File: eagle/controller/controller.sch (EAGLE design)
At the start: 6 parts, among them IC1 ATMEGA48/88/168-PU, IC2 LP2950ACZ-5.0

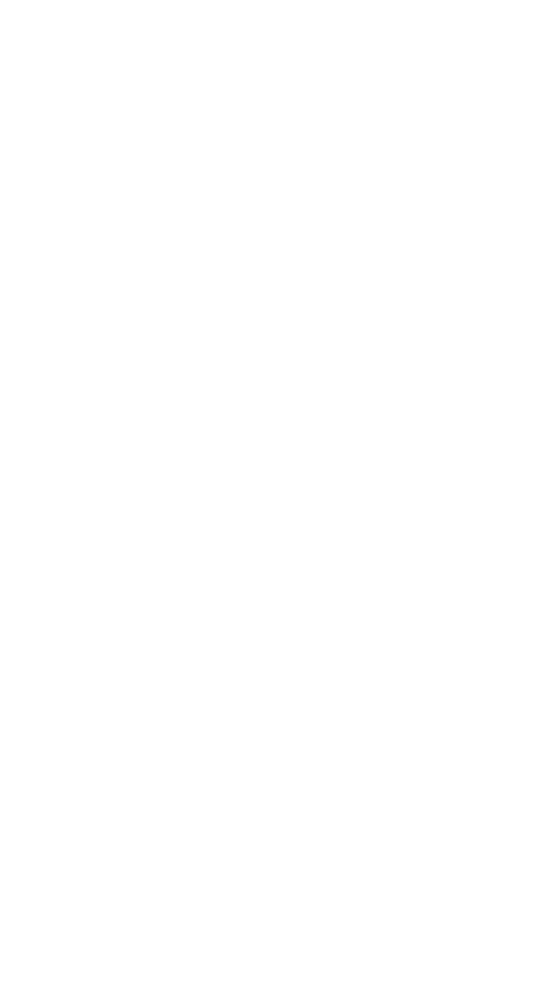
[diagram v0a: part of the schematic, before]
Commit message: Added REED for sensor switches
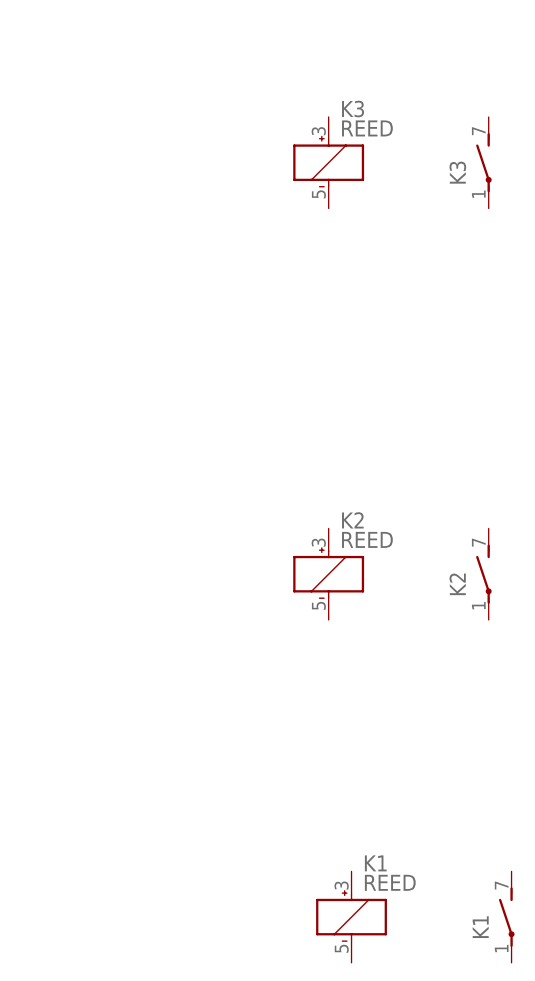
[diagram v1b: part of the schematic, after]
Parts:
- added K1, K2, K3: REED, relay:REED
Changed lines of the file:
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@@
 <part name="C2" library="resistor" deviceset="CPOL-EU" device="E2.5-7" value="10u"/>
 <part name="C3" library="resistor" deviceset="CPOL-EU" device="E2.5-7" value="10u"/>
+<part name="K1" library="relay" deviceset="REED" device=""/>
+<part name="K2" library="relay" deviceset="REED" device=""/>
+<part name="K3" library="relay" deviceset="REED" device=""/>
 </parts>
 <sheets>
@@
 <instance part="C2" gate="G$1" x="-27.94" y="68.58"/>
 <instance part="C3" gate="G$1" x="-55.88" y="68.58"/>
+<instance part="K1" gate="2" x="208.28" y="-5.08"/>
+<instance part="K1" gate="1" x="190.5" y="-5.08"/>
+<instance part="K2" gate="2" x="205.74" y="33.02"/>
+<instance part="K2" gate="1" x="187.96" y="33.02"/>
+<instance part="K3" gate="2" x="205.74" y="78.74"/>
+<instance part="K3" gate="1" x="187.96" y="78.74"/>
 </instances>
 <busses>

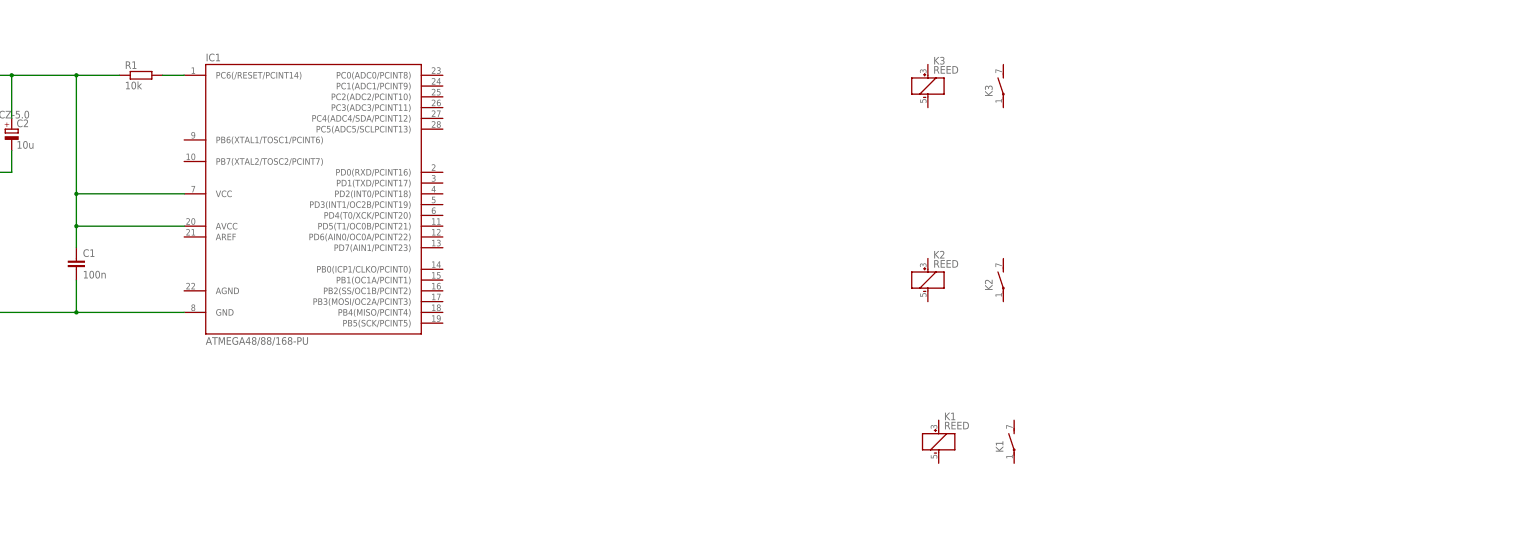
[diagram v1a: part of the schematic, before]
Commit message: Added base water sensors
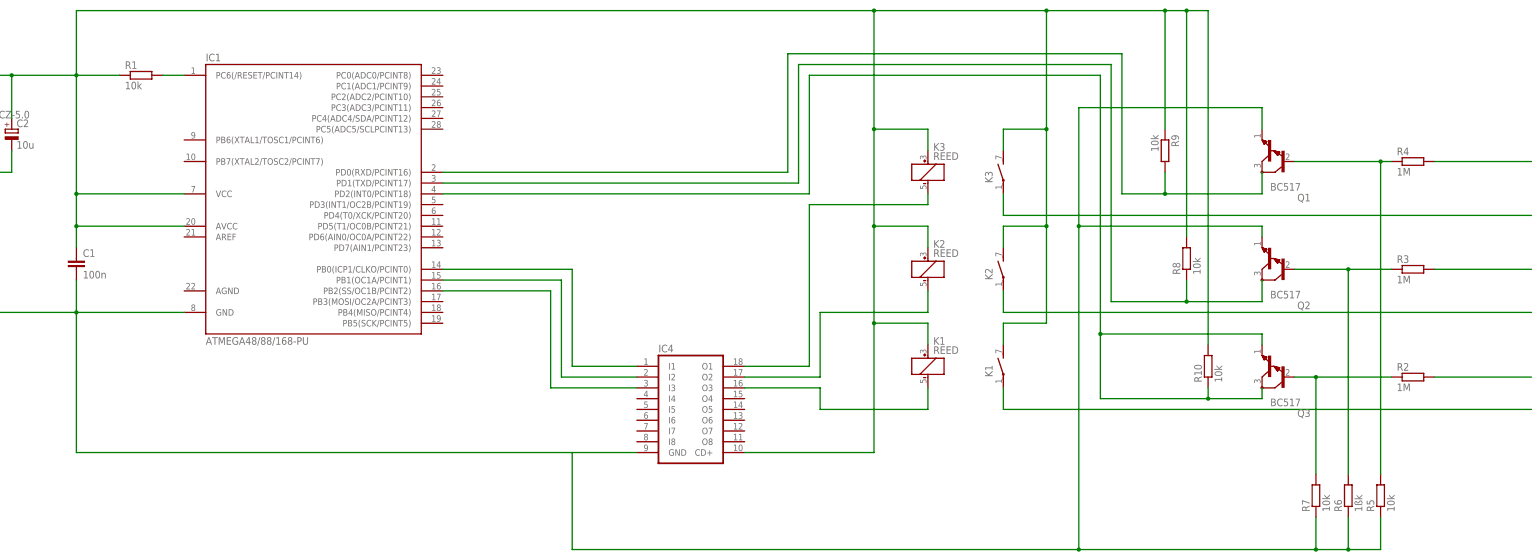
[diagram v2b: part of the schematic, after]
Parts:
- added IC4: (no value), uln-udn:ULN2803A
- added Q1, Q2, Q3: BC517, transistor-npn:BC517
- added R10, R5, R7, R8, R9: 10k, resistor:R-EU_0204/7
- added R2, R3, R4: 1M, resistor:R-EU_0204/7
- added R6: 1ßk, resistor:R-EU_0204/7
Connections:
- removed net N$1: C1.1, C2.+, IC1.AVCC, IC1.VCC@1, IC2.OUT, R1.1
- new net N$10: K22.P
- new net N$11: K12.P
- new net N$12: Q3.B, R2.1, R7.2
- new net N$13: Q2.B, R3.1, R6.2
- new net N$14: Q1.B, R4.1, R5.2
- new net N$15: R4.2
- new net N$16: R3.2
- new net N$17: R2.2
- new net N$18: C1.1, C2.+, IC1.AVCC, IC1.VCC@1, IC2.OUT, IC4.CD+, K11.+, K12.S, K21.+, K22.S, K31.+, K32.S, R1.1, R10.2, R8.2, R9.1
- new net N$19: IC1.PD0(RXD/PCINT16), Q1.C, R9.2
- new net N$22: IC1.PD1(TXD/PCINT17), Q2.C, R8.1
- new net N$23: IC1.PD2(INT0/PCINT18), Q3.C, Q3.E, R10.1
- new net N$3: IC4.O3, K11.-
- new net N$4: IC4.O2, K21.-
- new net N$5: IC4.O1, K31.-
- new net N$6: IC1.PB0(ICP1/CLKO/PCINT0), IC4.I1
- new net N$7: IC1.PB1(OC1A/PCINT1), IC4.I2
- new net N$8: IC1.PB2(SS/OC1B/PCINT2), IC4.I3
- new net N$9: K32.P
- net GND: now also IC4.GND, Q1.E, Q2.E, R5.1, R6.1, R7.1
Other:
- moved on the sheet: K1, K2, K3
